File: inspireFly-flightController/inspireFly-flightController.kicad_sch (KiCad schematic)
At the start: 15 parts, among them SW2 SW_Push, U1 STM32U595VITx

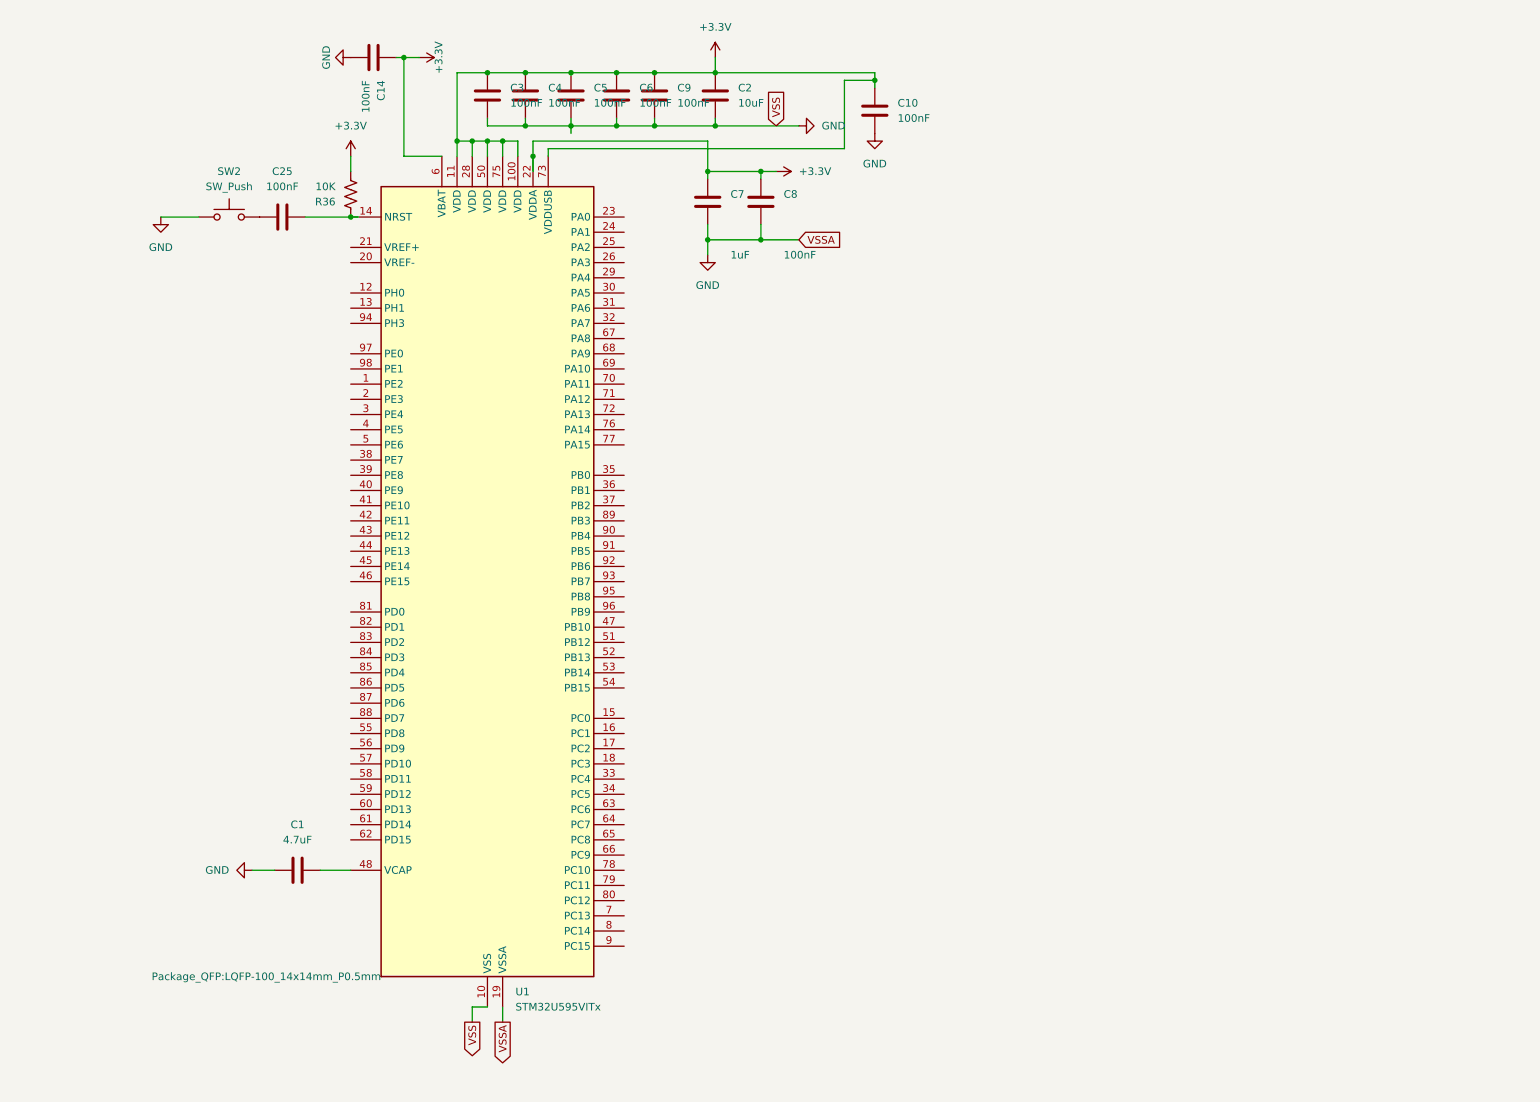
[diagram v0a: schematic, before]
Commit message: Slight changes
Removed cap on VBat
Added 1uF and 100nF to VREF+
Removed excess labels
Cleaned up labels
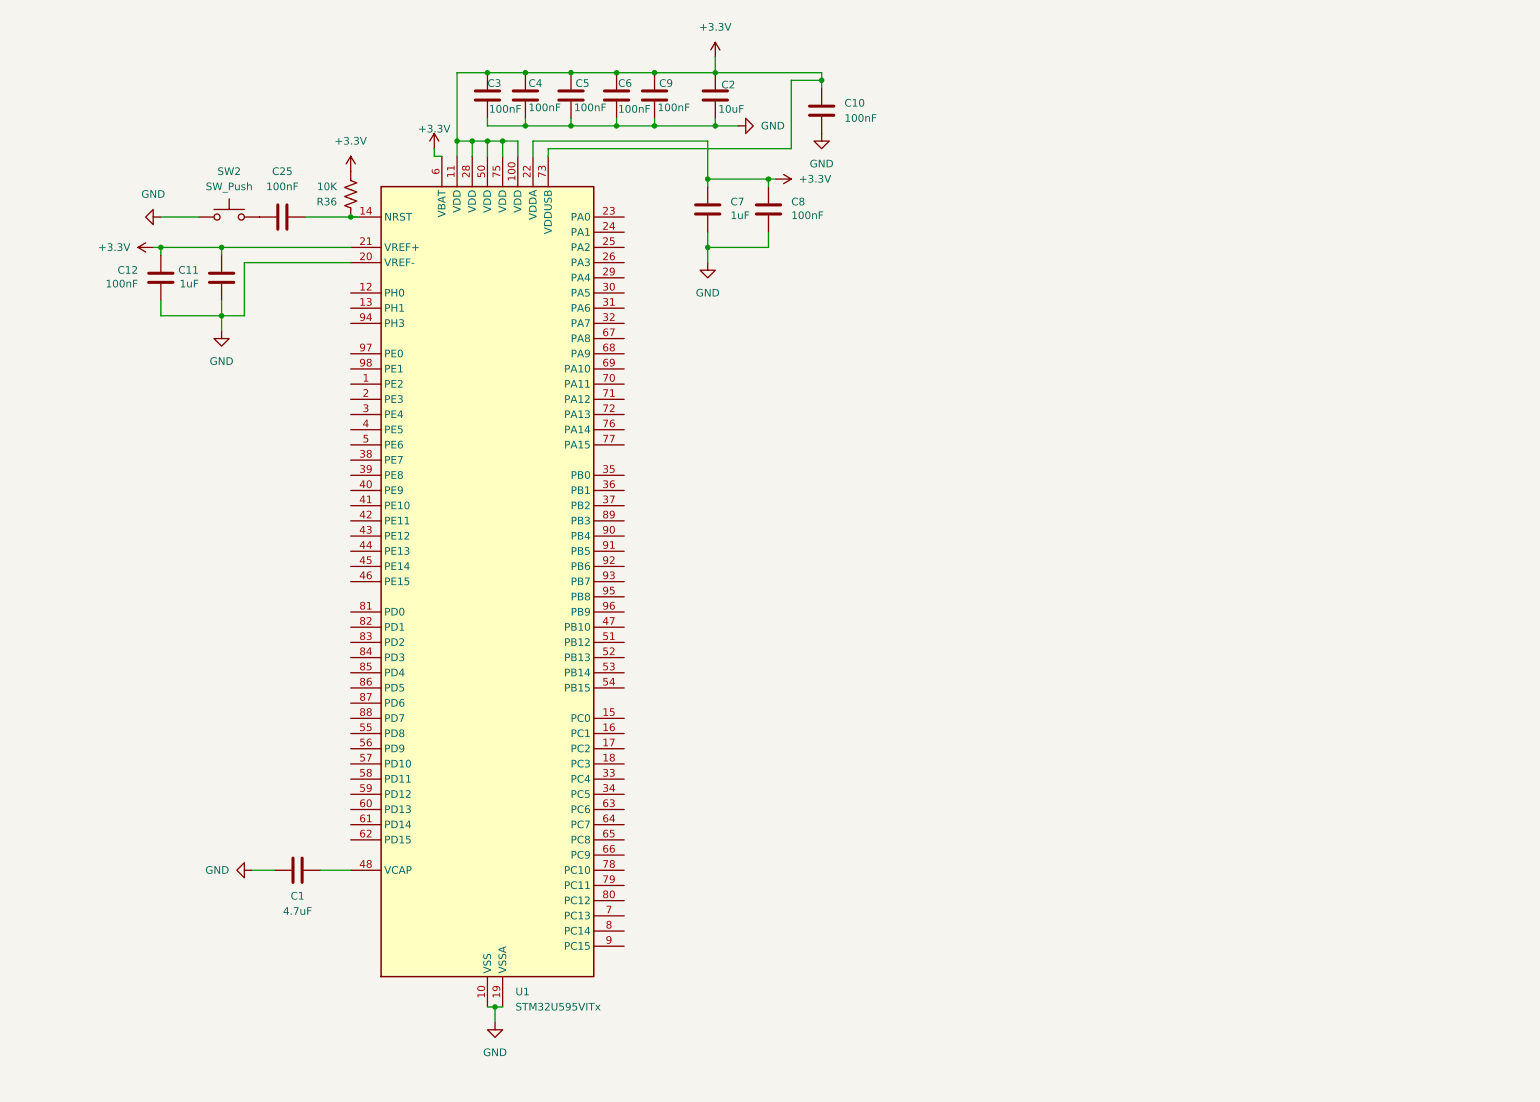
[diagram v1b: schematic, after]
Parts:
- removed C14: 100nF, Capacitor_SMD:C_0402_1005Metric_Pad0.74x0.62mm_HandSolder, symbol Device:C
- added C11: 1uF, Capacitor_SMD:C_0402_1005Metric_Pad0.74x0.62mm_HandSolder, symbol Device:C
- added C12: 100nF, Capacitor_SMD:C_0402_1005Metric_Pad0.74x0.62mm_HandSolder, symbol Device:C
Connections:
- net +3.3V: now also U1.21 (VREF+), C11.1, C12.1
- net GND: now also U1.20 (VREF-), C11.2, C12.2
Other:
- moved on the sheet: C10, C7, C8

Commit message: added Boot and crystal
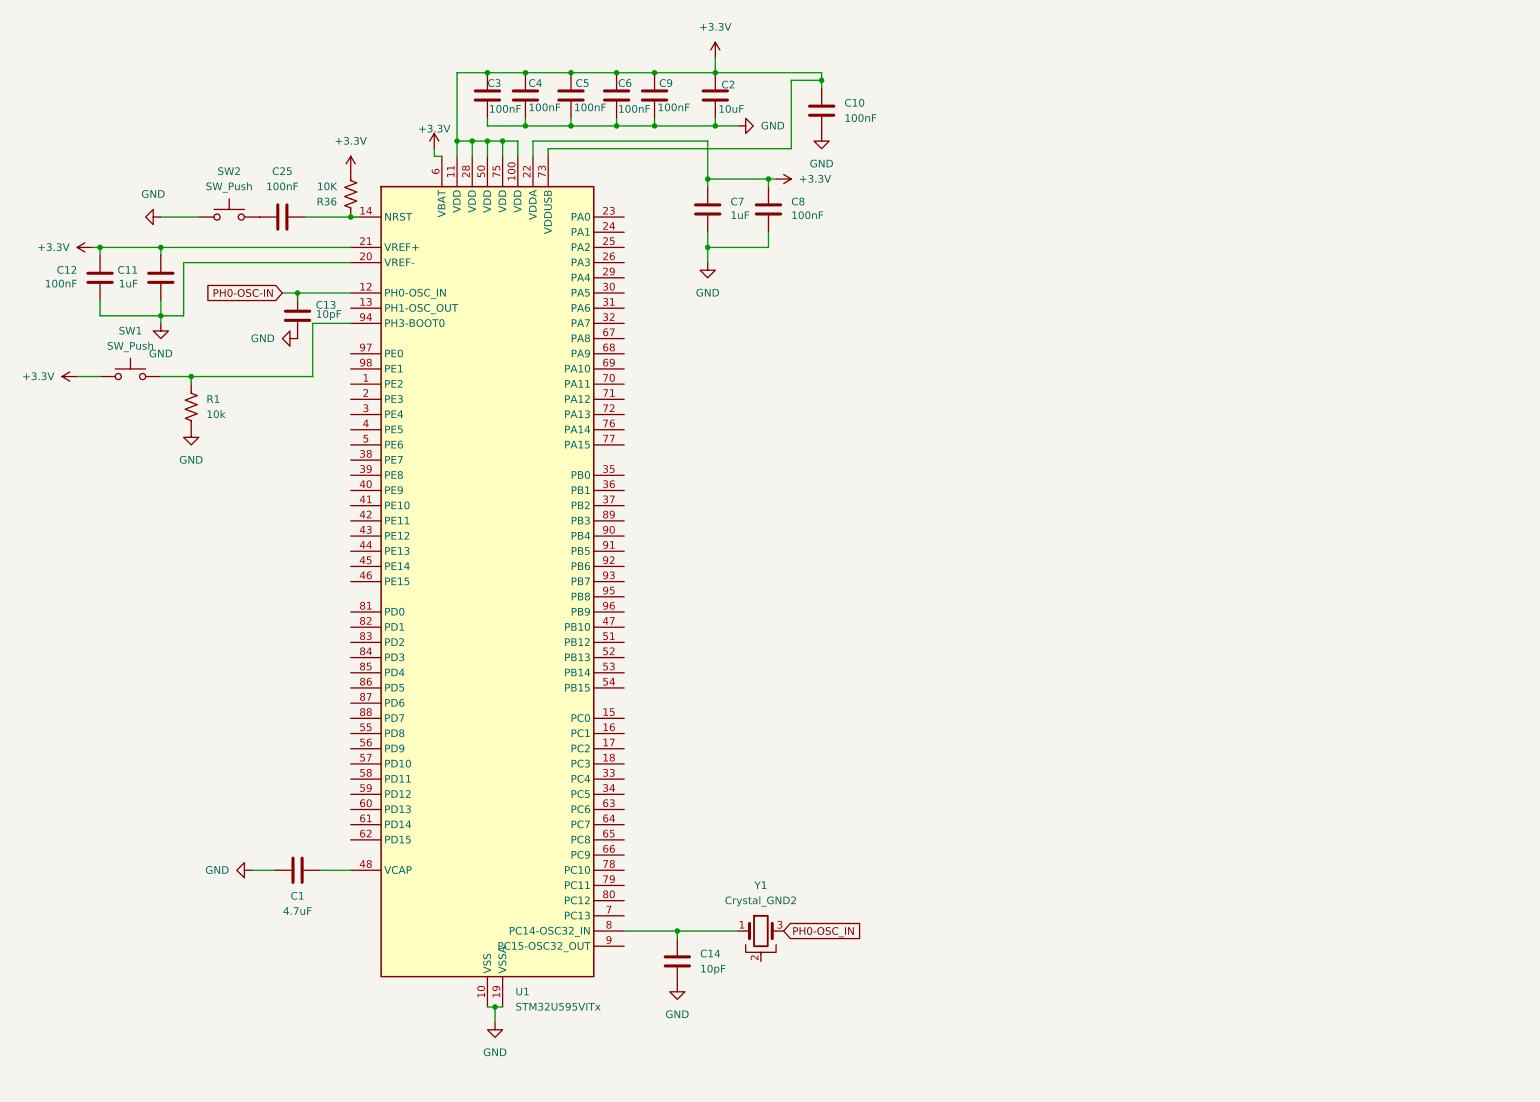
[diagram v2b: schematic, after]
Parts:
- added C13, C14: 10pF, symbol Device:C
- added R1: 10k, symbol Device:R_US
- added SW1: SW_Push, symbol Switch:SW_Push
- added Y1: Crystal_GND2, symbol Device:Crystal_GND2
- U1: symbol MCU_ST_STM32U5:STM32U595VITx -> flightController:STM32U595VITx
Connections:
- net +3.3V: now also SW1.1
- net GND: now also C13.2, C14.2, R1.2
- net PH0-OSC-IN: now reaches U1.12 (PH0-OSC_IN)
- net PH0-OSC-IN: now also C13.1
- net at U1.8 (PC14-OSC32_IN): now also C14.1, Y1.1
- net at U1.94 (PH3-BOOT0): now also R1.1, SW1.2
- new net PH0-OSC_IN: Y1.3
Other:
- moved on the sheet: C11, C12

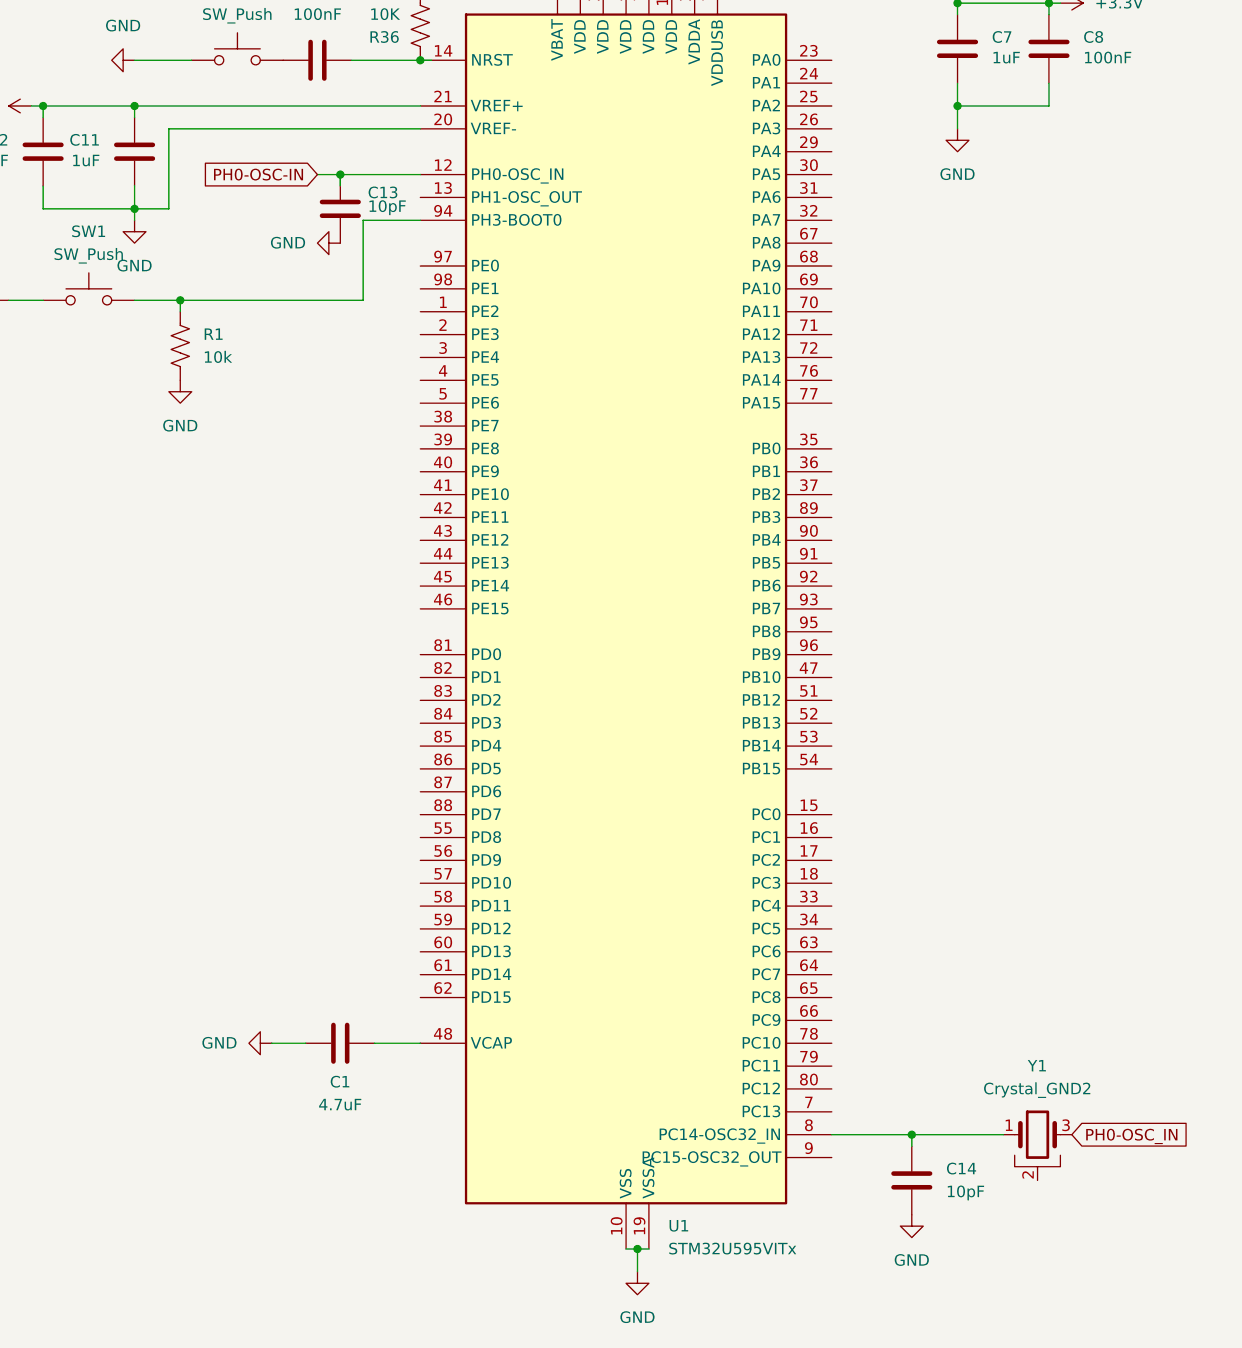
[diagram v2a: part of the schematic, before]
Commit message: added 32kHz OSC
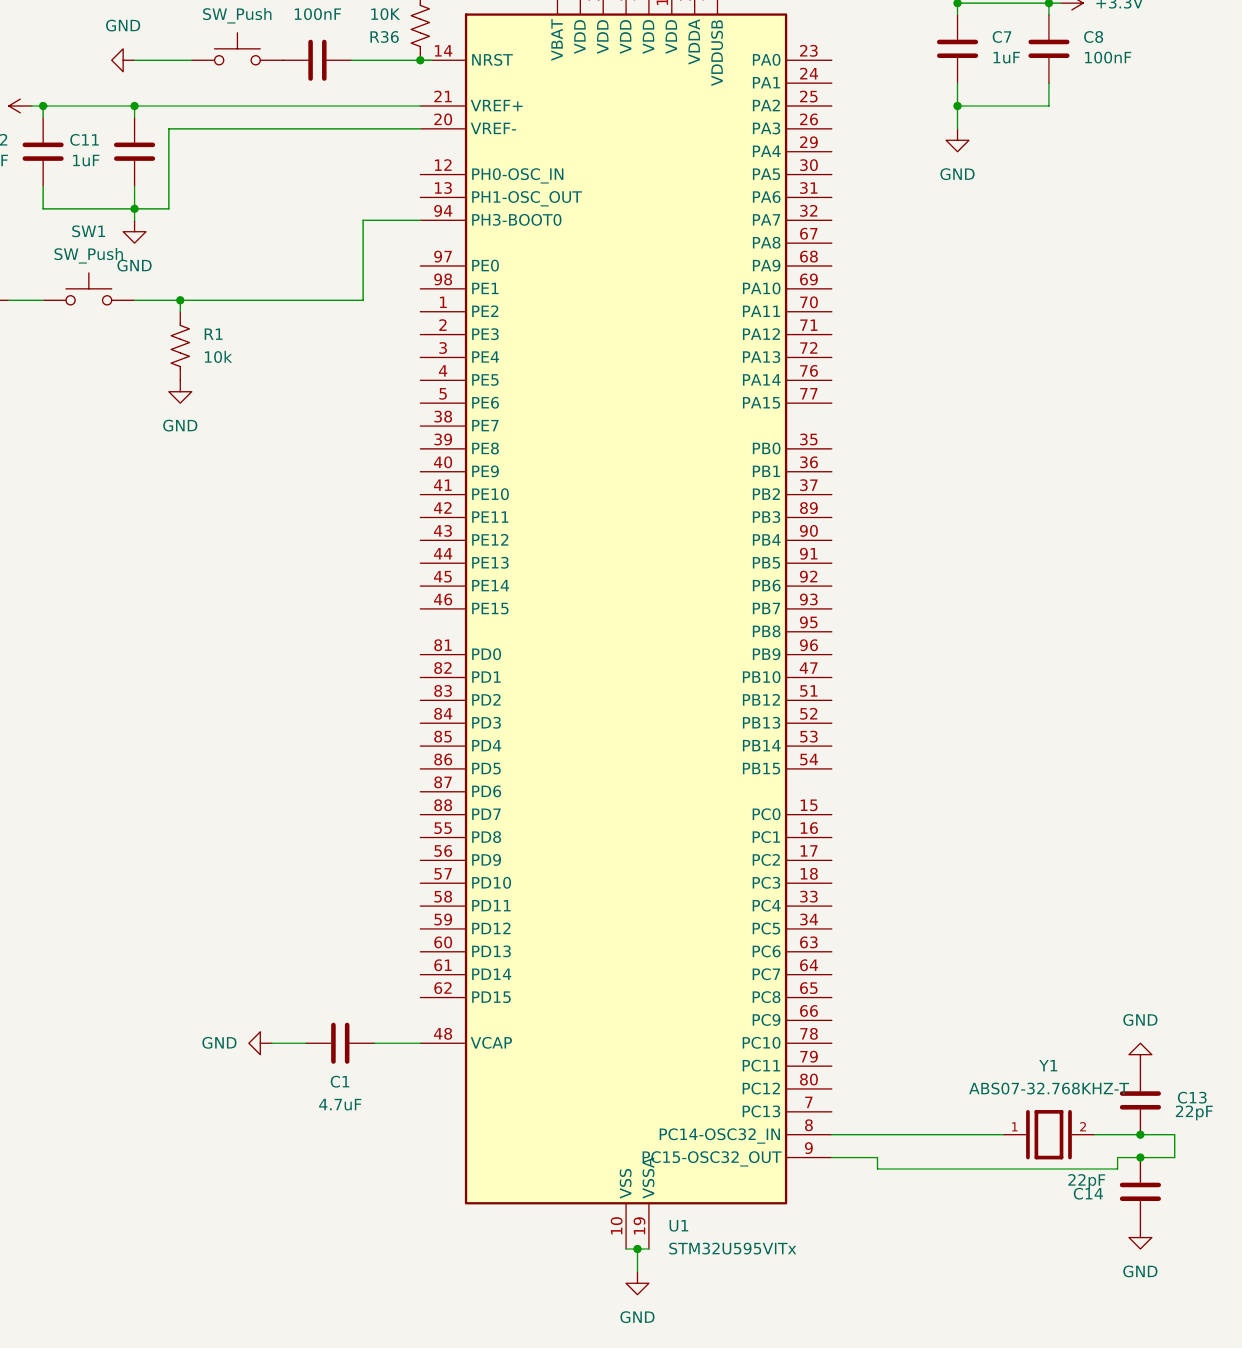
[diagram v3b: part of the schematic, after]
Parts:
- removed Y1: Crystal_GND2, symbol Device:Crystal_GND2
- added Y1: ABS07-32.768KHZ-T, ABS07-32.768KHZ-T:XTAL_ABS07-32.768KHZ-T, symbol flightController:ABS07-32.768KHZ-T
- C13, C14: value 10pF -> 22pF
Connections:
- net GND: now also C13.1, C14.1; no longer C13.2, C14.2
- net at U1.8 (PC14-OSC32_IN): now also Y1.1; no longer C14.1
- net at U1.9 (PC15-OSC32_OUT): now also C13.2, C14.2, Y1.2
- net PH0-OSC-IN: no longer names the net of U1.12 (PH0-OSC_IN)
- net PH0-OSC-IN: no longer C13.1
